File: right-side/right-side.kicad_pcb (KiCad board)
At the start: 2 copper layers, 165 x 90 mm, 0 parts

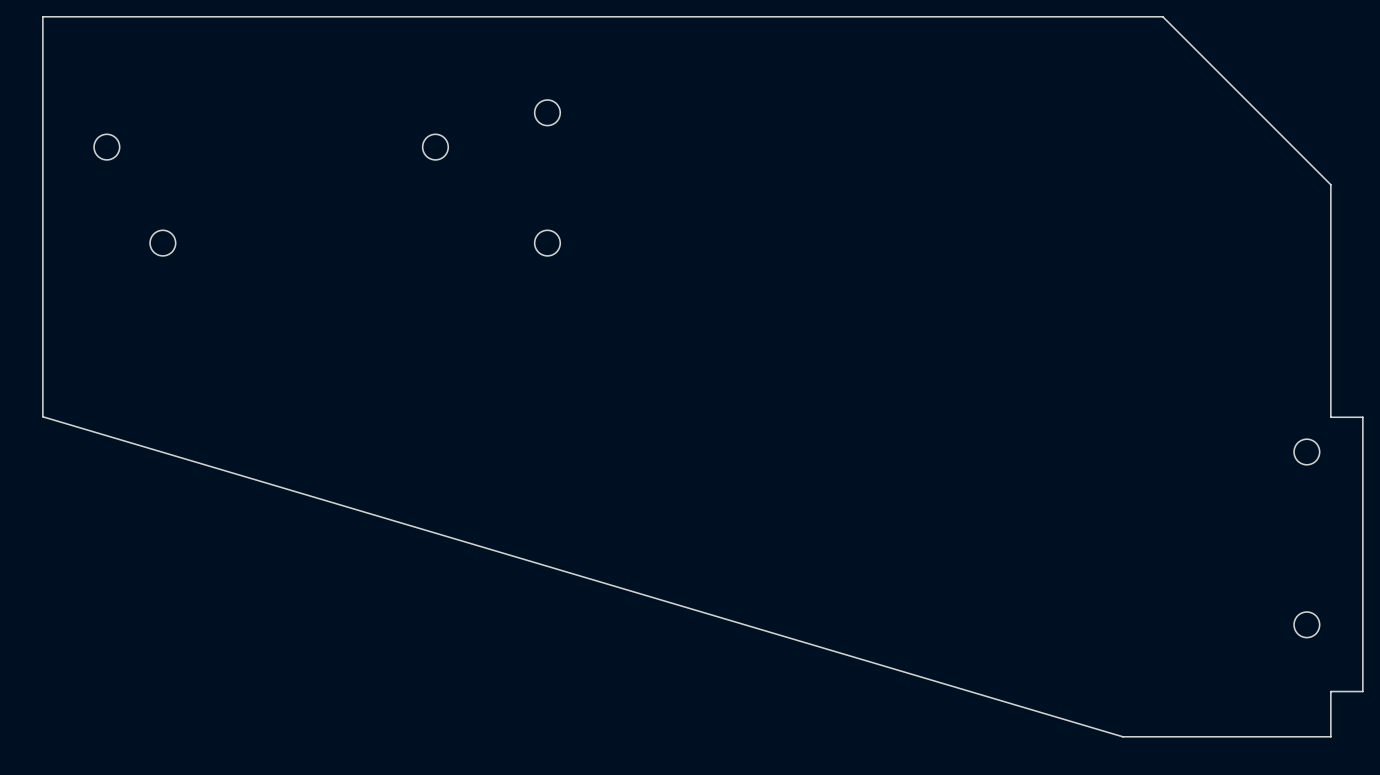
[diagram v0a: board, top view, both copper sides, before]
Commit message: update outlines, finish left side
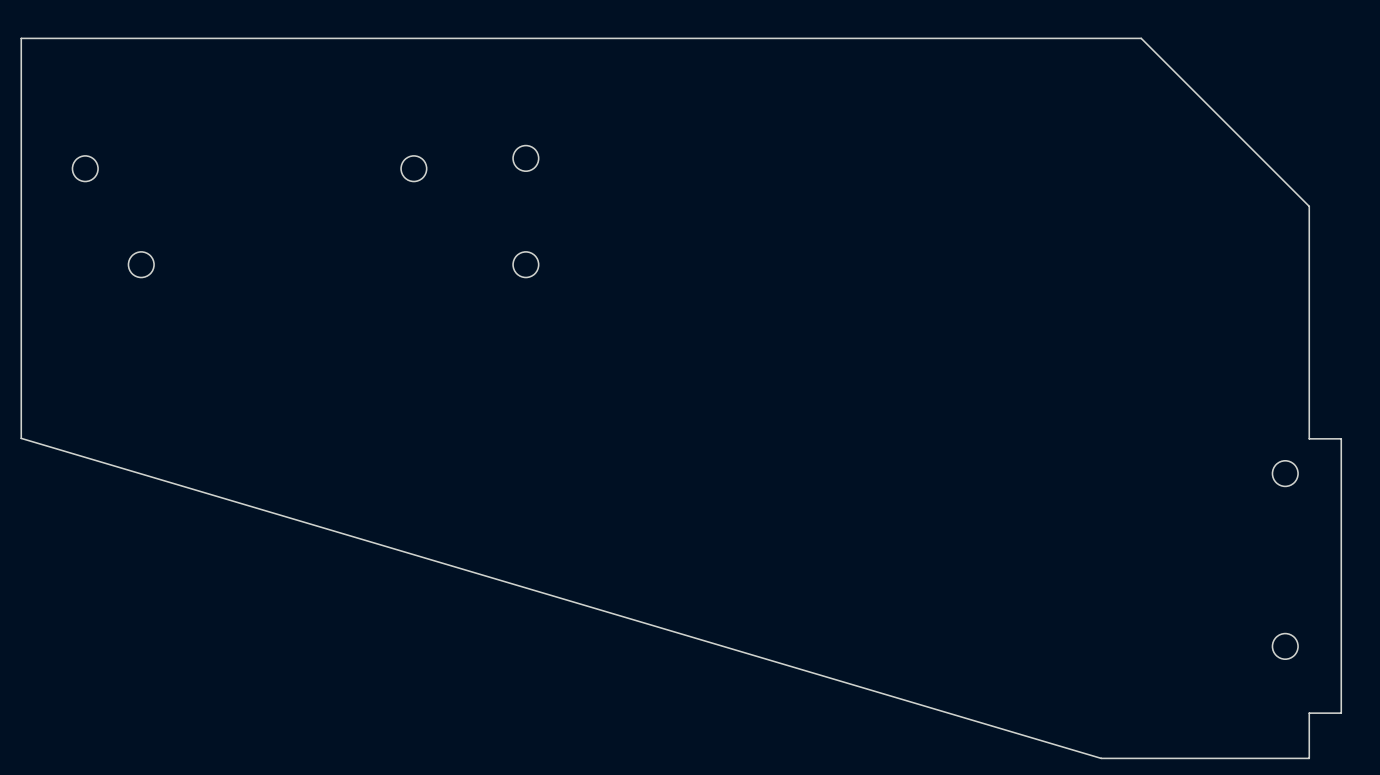
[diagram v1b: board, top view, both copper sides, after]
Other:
- outline, holes or cut-outs redrawn
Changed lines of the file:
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@@
   )
   (net 0 "")
-  (gr_line (start 216.708 53.086) (end 76.708 53.086)
+  (gr_line (start 235.008628 105.842127) (end 235.008628 76.785273)
     (stroke (width 0.2) (type solid)) (layer "Edge.Cuts"))
-  (gr_line (start 241.708 103.142854) (end 237.708 103.142854)
+  (gr_circle (center 137.084 70.785273) (end 138.684 70.785273)
+    (stroke (width 0.2) (type solid)) (fill none) (layer "Edge.Cuts"))
+  (gr_circle (center 89.008628 84.074) (end 90.608628 84.074)
+    (stroke (width 0.2) (type solid)) (fill none) (layer "Edge.Cuts"))
+  (gr_line (start 235.008628 145.785273) (end 235.008628 140.128419)
     (stroke (width 0.2) (type solid)) (layer "Edge.Cuts"))
-  (gr_line (start 237.708 143.086) (end 237.708 137.429146)
+  (gr_line (start 235.008628 140.128419) (end 239.008628 140.128419)
     (stroke (width 0.2) (type solid)) (layer "Edge.Cuts"))
-  (gr_line (start 211.708 143.086) (end 237.708 143.086)
+  (gr_line (start 239.008628 105.842127) (end 235.008628 105.842127)
     (stroke (width 0.2) (type solid)) (layer "Edge.Cuts"))
-  (gr_circle (center 91.708 81.374727) (end 93.308 81.374727)
+  (gr_line (start 214.008628 55.785273) (end 74.008628 55.785273)
+    (stroke (width 0.2) (type solid)) (layer "Edge.Cuts"))
+  (gr_line (start 74.008628 55.785273) (end 74.008628 105.785273)
+    (stroke (width 0.2) (type solid)) (layer "Edge.Cuts"))
+  (gr_circle (center 232.008628 131.785273) (end 233.608628 131.785273)
     (stroke (width 0.2) (type solid)) (fill none) (layer "Edge.Cuts"))
-  (gr_line (start 237.708 103.142854) (end 237.708 74.086)
+  (gr_circle (center 137.084 84.074) (end 138.684 84.074)
+    (stroke (width 0.2) (type solid)) (fill none) (layer "Edge.Cuts"))
+  (gr_line (start 74.008628 105.785273) (end 209.008628 145.785273)
     (stroke (width 0.2) (type solid)) (layer "Edge.Cuts"))
-  (gr_circle (center 139.783372 65.086) (end 141.383372 65.086)
+  (gr_line (start 209.008628 145.785273) (end 235.008628 145.785273)
+    (stroke (width 0.2) (type solid)) (layer "Edge.Cuts"))
+  (gr_line (start 239.008628 140.128419) (end 239.008628 105.842127)
+    (stroke (width 0.2) (type solid)) (layer "Edge.Cuts"))
+  (gr_circle (center 232.008628 110.185273) (end 233.608628 110.185273)
     (stroke (width 0.2) (type solid)) (fill none) (layer "Edge.Cuts"))
-  (gr_line (start 76.708 103.086) (end 211.708 143.086)
+  (gr_circle (center 123.084 72.074) (end 124.684 72.074)
+    (stroke (width 0.2) (type solid)) (fill none) (layer "Edge.Cuts"))
+  (gr_circle (center 82.008628 72.074) (end 83.608628 72.074)
+    (stroke (width 0.2) (type solid)) (fill none) (layer "Edge.Cuts"))
+  (gr_line (start 235.008628 76.785273) (end 214.008628 55.785273)
     (stroke (width 0.2) (type solid)) (layer "Edge.Cuts"))
-  (gr_line (start 237.708 74.086) (end 216.708 53.086)
-    (stroke (width 0.2) (type solid)) (layer "Edge.Cuts"))
-  (gr_circle (center 234.708 129.086) (end 236.308 129.086)
-    (stroke (width 0.2) (type solid)) (fill none) (layer "Edge.Cuts"))
-  (gr_circle (center 139.783372 81.374727) (end 141.383372 81.374727)
-    (stroke (width 0.2) (type solid)) (fill none) (layer "Edge.Cuts"))
-  (gr_circle (center 84.708 69.374727) (end 86.308 69.374727)
-    (stroke (width 0.2) (type solid)) (fill none) (layer "Edge.Cuts"))
-  (gr_line (start 237.708 137.429146) (end 241.708 137.429146)
-    (stroke (width 0.2) (type solid)) (layer "Edge.Cuts"))
-  (gr_line (start 76.708 53.086) (end 76.708 103.086)
-    (stroke (width 0.2) (type solid)) (layer "Edge.Cuts"))
-  (gr_line (start 241.708 137.429146) (end 241.708 103.142854)
-    (stroke (width 0.2) (type solid)) (layer "Edge.Cuts"))
-  (gr_circle (center 125.783372 69.374727) (end 127.383372 69.374727)
-    (stroke (width 0.2) (type solid)) (fill none) (layer "Edge.Cuts"))
-  (gr_circle (center 234.708 107.486) (end 236.308 107.486)
-    (stroke (width 0.2) (type solid)) (fill none) (layer "Edge.Cuts"))
 )

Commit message: finalize both panels
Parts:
- added A1: Buck, right-side:Buck, F.Cu at (176.3, 83.6)
- added A3: Buck, right-side:Buck, F.Cu at (176.3, 108.0)
- added C1: 0.1uF, Capacitor_THT:C_Disc_D5.0mm_W2.5mm_P5.00mm, F.Cu at (106.5, 95.2)
- added C2: 0.1uF, Capacitor_THT:C_Disc_D5.0mm_W2.5mm_P5.00mm, F.Cu at (123.6, 100.3)
- added J1: XT60, Connector_AMASS:AMASS_XT60-M_1x02_P7.20mm_Vertical, B.Cu at (214.6, 66.6)
- added J10: Pixhawk Power, Connector_Hirose:Hirose_DF13-06P-1.25DSA_1x06_P1.25mm_Vertical, F.Cu at (120.3, 96.5)
- added J2: XT60, Connector_AMASS:AMASS_XT60-F_1x02_P7.20mm_Vertical, F.Cu at (211.5, 86.1)
- added J3: XT60, Connector_AMASS:AMASS_XT60-F_1x02_P7.20mm_Vertical, F.Cu at (211.5, 96.0)
- added J4: Servo Power, Connector_PinHeader_2.54mm:PinHeader_1x03_P2.54mm_Vertical, F.Cu at (142.5, 95.5)
- added J5: XT60, Connector_AMASS:AMASS_XT60-F_1x02_P7.20mm_Vertical, F.Cu at (211.5, 105.9)
- added J6: Motor Battery, Connector_PinHeader_2.54mm:PinHeader_1x03_P2.54mm_Vertical, F.Cu at (141.0, 107.4)
- added J7: Pixhawk 6.6V ADC, Connector_Hirose:Hirose_DF13-03P-1.25DSA_1x03_P1.25mm_Vertical, F.Cu at (97.1, 96.5)
- added J8: RFD (PX side), Connector_Hirose:Hirose_DF13-06P-1.25DSA_1x06_P1.25mm_Vertical, F.Cu at (80.3, 96.5)
- added J9: RFD, Connector_PinHeader_2.54mm:PinHeader_1x06_P2.54mm_Vertical, F.Cu at (214.1, 141.5)
- added R1: 100K, Resistor_THT:R_Axial_DIN0207_L6.3mm_D2.5mm_P10.16mm_Horizontal, F.Cu at (114.0, 101.9)
- added R2: 10K, Resistor_THT:R_Axial_DIN0207_L6.3mm_D2.5mm_P10.16mm_Horizontal, F.Cu at (103.9, 98.6)
- added R3: 10K, Resistor_THT:R_Axial_DIN0207_L6.3mm_D2.5mm_P10.16mm_Horizontal, F.Cu at (121.0, 103.6)
- added R4: 91K, Resistor_THT:R_Axial_DIN0207_L6.3mm_D2.5mm_P10.16mm_Horizontal, F.Cu at (131.1, 106.9)
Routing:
- net GND: track 0.00 -> 227.5 mm
- net +BATT: track 0.00 -> 163.4 mm
- net Net-(J8-Pin_2): track 0.00 -> 158.4 mm
- net Net-(J8-Pin_3): track 0.00 -> 157.6 mm
- net Net-(J8-Pin_1): track 0.00 -> 157.2 mm
- net Net-(J8-Pin_5): track 0.00 -> 156.2 mm, vias 0 -> 2
- net Net-(J8-Pin_4): track 0.00 -> 149.6 mm, vias 0 -> 1
- net Net-(J8-Pin_6): track 0.00 -> 140.6 mm
- net Net-(J6-Pin_3): track 0.00 -> 57.1 mm
- net Net-(A3-VOUT): track 0.00 -> 45.7 mm
- net Net-(J6-Pin_2): track 0.00 -> 31.9 mm
- net Net-(J7-Pin_2): track 0.00 -> 14.8 mm
- net Net-(A1-VOUT): track 0.00 -> 13.0 mm
- net Net-(J10-Pin_4): track 0.00 -> 11.7 mm
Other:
- outline, holes or cut-outs redrawn
- board text added: "+5.5V"
- board text added: "+5V"
- board text added: "+BATT"
- board text added: "-BATT"
- board text added: "5V"
- board text added: "AVALON X"
- board text added: "CTS"
- board text added: "Electronics Bay Right Panel v1 Alan Hsu"
- board text added: "Extra in case we fuck up"
- board text added: "GND"
- board text added: "Input from Left Side Panel"
- board text added: "Monitor"
- board text added: "RTS"
- board text added: "RX"
- board text added: "TX"
- board text added: "To Gimbal"
- board text added: "To POE Injector"
